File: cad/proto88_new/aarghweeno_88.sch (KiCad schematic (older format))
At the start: 28 parts, among them J1 Screw_Terminal_01x02, J2 AVR-ISP-6, J23 Vin Conn, J3 Conn_01x38_Male, U1 LM7805_TO220, U2 Atmega8_dip, Y1 16MHz

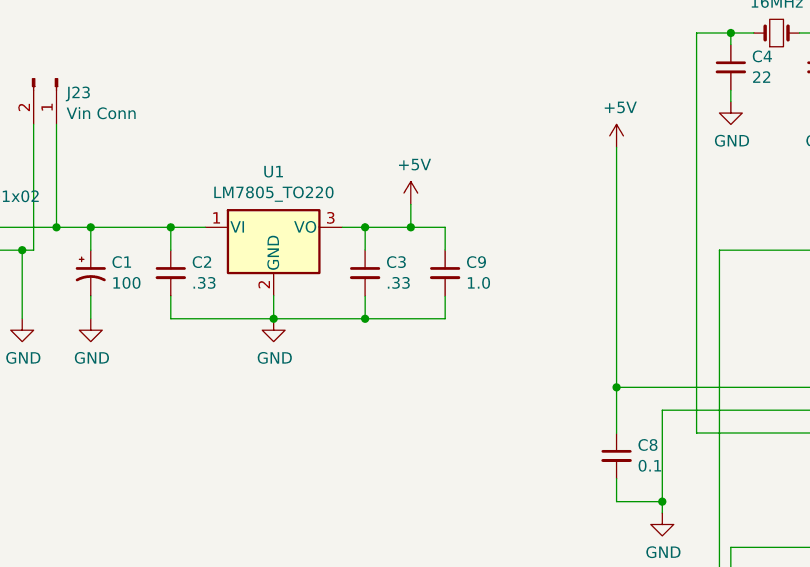
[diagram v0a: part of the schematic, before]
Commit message: Changed reg cap value, changed version, added port# to LED, cleaned up silkscreen.
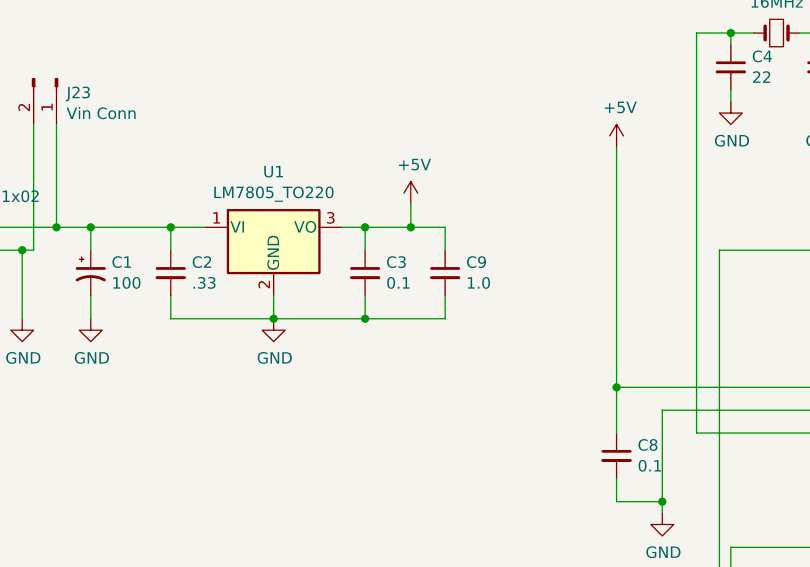
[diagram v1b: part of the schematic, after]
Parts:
- C3: value .33 -> 0.1
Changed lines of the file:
@@
 Sheet 1 2
 Title "ATMega8/88/168/328 Proto Board"
-Date "2022-07-17"
-Rev "0"
+Date "2022-08-07"
+Rev "1.1"
 Comp "Small Time Electronics"
 Comment1 ""
@@
 P 2700 1900
 F 0 "C3" H 2792 1946 50  0000 L CNN
-F 1 ".33" H 2792 1855 50  0000 L CNN
+F 1 "0.1" H 2792 1855 50  0000 L CNN
 F 2 "Capacitor_THT:C_Disc_D5.0mm_W2.5mm_P5.00mm" H 2700 1900 50  0001 C CNN
 F 3 "~" H 2700 1900 50  0001 C CNN
